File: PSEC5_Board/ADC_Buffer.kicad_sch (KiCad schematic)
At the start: 36 parts, among them IC1 LTC6409IUDB#TRMPBF, IC2 LTC6409IUDB#TRMPBF, IC4 LTC6409IUDB#TRMPBF

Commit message: Added Footprints to Schematic
Added footprints to schematic, should be able to now update the layout design and have all nets be present
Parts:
- C35, C36, C37, C38, C39, C40, C41, C42, C43, C44, C45, C46, C47, C48, C49, C50, C51, C68, C70, C72, C73: footprint (none) -> Capacitor_SMD:C_0603_1608Metric
- IC1, IC2, IC4: footprint footprints:QFN-10_UDB_LIT -> LTC6409IUDB_TRMPBF:QFN-10_UDB_LIT
- R21, R22, R23, R24, R26, R27, R28, R29, R34, R36, R38, R40: footprint (none) -> Resistor_SMD:R_0603_1608Metric
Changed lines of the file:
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@@
 			)
 		)
-		(property "Footprint" ""
+		(property "Footprint" "Resistor_SMD:R_0603_1608Metric"
 			(at 58.166 128.016 90)
 			(effects
@@
 			)
 		)
-		(property "Footprint" ""
+		(property "Footprint" "Capacitor_SMD:C_0603_1608Metric"
 			(at 267.97 123.4948 0)
 			(effects
@@
 			)
 		)
-		(property "Footprint" ""
+		(property "Footprint" "Resistor_SMD:R_0603_1608Metric"
 			(at 36.576 148.336 90)
 			(effects
@@
 			)
 		)
-		(property "Footprint" ""
+		(property "Footprint" "Capacitor_SMD:C_0603_1608Metric"
 			(at 40.64 75.2348 0)
 			(effects
@@
 			)
 		)
-		(property "Footprint" ""
+		(property "Footprint" "Capacitor_SMD:C_0603_1608Metric"
 			(at 55.88 144.4752 0)
 			(effects
@@
 			)
 		)
-		(property "Footprint" ""
+		(property "Footprint" "Capacitor_SMD:C_0603_1608Metric"
 			(at 134.62 131.1148 0)
 			(effects
@@
 			)
 		)
-		(property "Footprint" "footprints:QFN-10_UDB_LIT"
+		(property "Footprint" "LTC6409IUDB_TRMPBF:QFN-10_UDB_LIT"
 			(at 241.3 176.2 0)
 			(effects
@@
 			)
 		)
-		(property "Footprint" ""
+		(property "Footprint" "Capacitor_SMD:C_0603_1608Metric"
 			(at 133.35 86.6648 0)
 			(effects
@@
 			)
 		)
-		(property "Footprint" ""
+		(property "Footprint" "Capacitor_SMD:C_0603_1608Metric"
 			(at 62.23 115.8748 0)
 			(effects
@@
 			)
 		)
-		(property "Footprint" ""
+		(property "Footprint" "Resistor_SMD:R_0603_1608Metric"
 			(at 60.706 73.914 90)
 			(effects
@@
 			)
 		)
-		(property "Footprint" ""
+		(property "Footprint" "Capacitor_SMD:C_0603_1608Metric"
 			(at 133.35 157.7848 0)
 			(effects
@@
 			)
 		)
-		(property "Footprint" ""
+		(property "Footprint" "Capacitor_SMD:C_0603_1608Metric"
 			(at 267.97 112.0648 0)
 			(effects
@@
 			)
 		)
-		(property "Footprint" ""
+		(property "Footprint" "Resistor_SMD:R_0603_1608Metric"
 			(at 45.466 49.276 90)
 			(effects
@@
 			)
 		)
-		(property "Footprint" ""
+		(property "Footprint" "Capacitor_SMD:C_0603_1608Metric"
 			(at 133.35 169.2148 0)
 			(effects
@@
 			)
 		)
-		(property "Footprint" ""
+		(property "Footprint" "Capacitor_SMD:C_0603_1608Metric"
 			(at 133.35 75.2348 0)
 			(effects
@@
 			)
 		)
-		(property "Footprint" ""
+		(property "Footprint" "Capacitor_SMD:C_0603_1608Metric"
 			(at 269.24 73.9648 0)
 			(effects
@@
 			)
 		)
-		(property "Footprint" ""
+		(property "Footprint" "Capacitor_SMD:C_0603_1608Metric"
 			(at 134.62 119.6848 0)
 			(effects
@@
 			)
 		)
-		(property "Footprint" ""
+		(property "Footprint" "Capacitor_SMD:C_0603_1608Metric"
 			(at 62.23 33.3248 0)
 			(effects
@@
 			)
 		)
-		(property "Footprint" ""
+		(property "Footprint" "Capacitor_SMD:C_0603_1608Metric"
 			(at 40.64 157.7848 0)
 			(effects
@@
 			)
 		)
-		(property "Footprint" "footprints:QFN-10_UDB_LIT"
+		(property "Footprint" "LTC6409IUDB_TRMPBF:QFN-10_UDB_LIT"
 			(at 106.68 139.37 0)
 			(effects
@@
 			)
 		)
-		(property "Footprint" ""
+		(property "Footprint" "Resistor_SMD:R_0603_1608Metric"
 			(at 58.166 45.466 90)
 			(effects
@@
 			)
 		)
-		(property "Footprint" ""
+		(property "Footprint" "Resistor_SMD:R_0603_1608Metric"
 			(at 195.326 110.744 90)
 			(effects
@@
 			)
 		)
-		(property "Footprint" ""
+		(property "Footprint" "Capacitor_SMD:C_0603_1608Metric"
 			(at 196.85 70.1548 0)
 			(effects
@@
 			)
 		)
-		(property "Footprint" ""
+		(property "Footprint" "Capacitor_SMD:C_0603_1608Metric"
 			(at 190.5 98.7552 0)
 			(effects
@@
 			)
 		)
-		(property "Footprint" ""
+		(property "Footprint" "Resistor_SMD:R_0603_1608Metric"
 			(at 36.576 65.786 90)
 			(effects
@@
 			)
 		)
-		(property "Footprint" ""
+		(property "Footprint" "Capacitor_SMD:C_0603_1608Metric"
 			(at 175.26 112.0648 0)
 			(effects
@@
 			)
 		)
-		(property "Footprint" ""
+		(property "Footprint" "Resistor_SMD:R_0603_1608Metric"
 			(at 180.086 86.106 90)
 			(effects
@@
 			)
 		)
-		(property "Footprint" ""
+		(property "Footprint" "Resistor_SMD:R_0603_1608Metric"
 			(at 60.706 156.464 90)
 			(effects
@@
 			)
 		)
-		(property "Footprint" ""
+		(property "Footprint" "Resistor_SMD:R_0603_1608Metric"
 			(at 192.786 82.296 90)
 			(effects
@@
 			)
 		)
-		(property "Footprint" ""
+		(property "Footprint" "Capacitor_SMD:C_0603_1608Metric"
 			(at 269.24 85.3948 0)
 			(effects
@@
 			)
 		)
-		(property "Footprint" ""
+		(property "Footprint" "Capacitor_SMD:C_0603_1608Metric"
 			(at 134.62 37.1348 0)
 			(effects
@@
 			)
 		)
-		(property "Footprint" ""
+		(property "Footprint" "Capacitor_SMD:C_0603_1608Metric"
 			(at 55.88 61.9252 0)
 			(effects
@@
 			)
 		)
-		(property "Footprint" ""
+		(property "Footprint" "Capacitor_SMD:C_0603_1608Metric"
 			(at 134.62 48.5648 0)
 			(effects
@@
 			)
 		)
-		(property "Footprint" ""
+		(property "Footprint" "Resistor_SMD:R_0603_1608Metric"
 			(at 171.196 102.616 90)
 			(effects
@@
 			)
 		)
-		(property "Footprint" ""
+		(property "Footprint" "Resistor_SMD:R_0603_1608Metric"
 			(at 45.466 131.826 90)
 			(effects
@@
 			)
 		)
-		(property "Footprint" "footprints:QFN-10_UDB_LIT"
+		(property "Footprint" "LTC6409IUDB_TRMPBF:QFN-10_UDB_LIT"
 			(at 106.68 221.92 0)
 			(effects

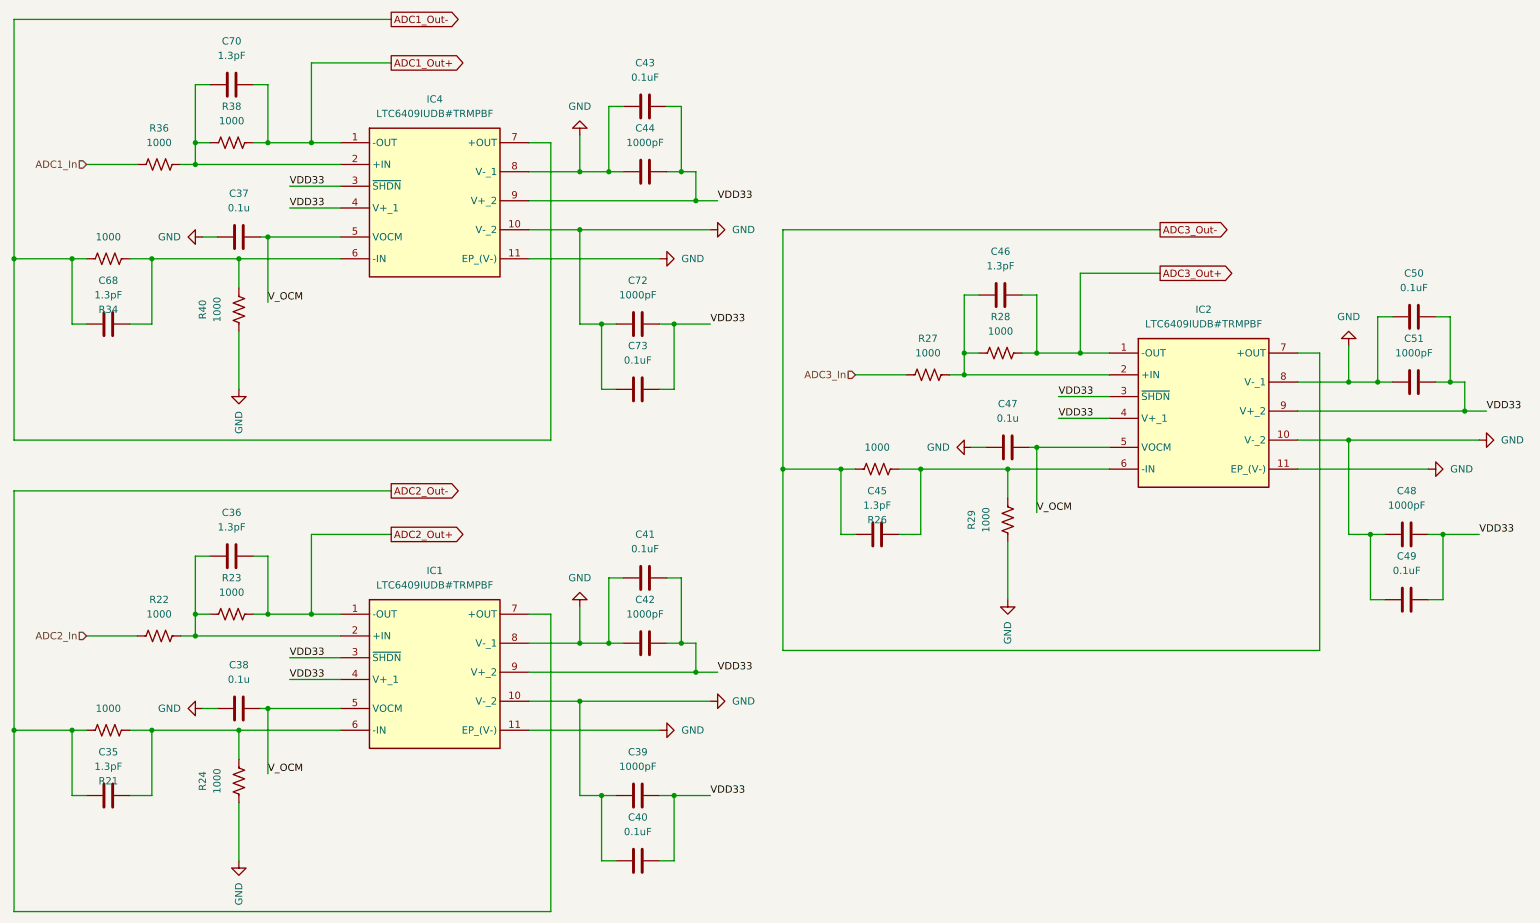
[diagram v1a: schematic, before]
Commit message: DUT Layout Overhaul
Footprints need to be replaced.
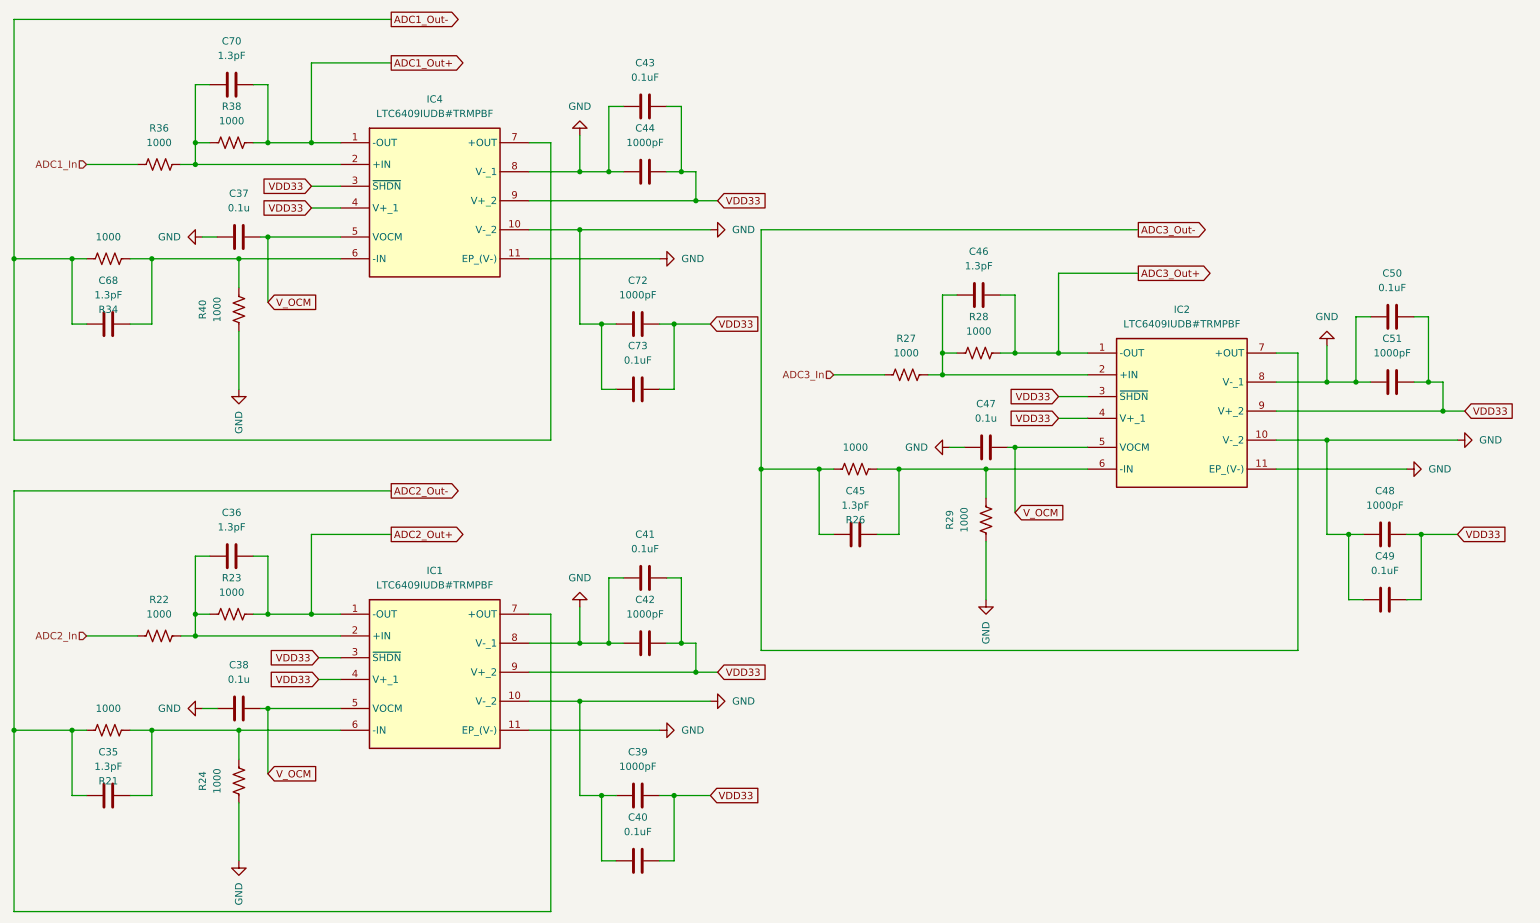
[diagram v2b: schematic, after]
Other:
- moved on the sheet: C45, C46, C47, C48, C49, C50, C51, IC2, R26, R27, R28, R29

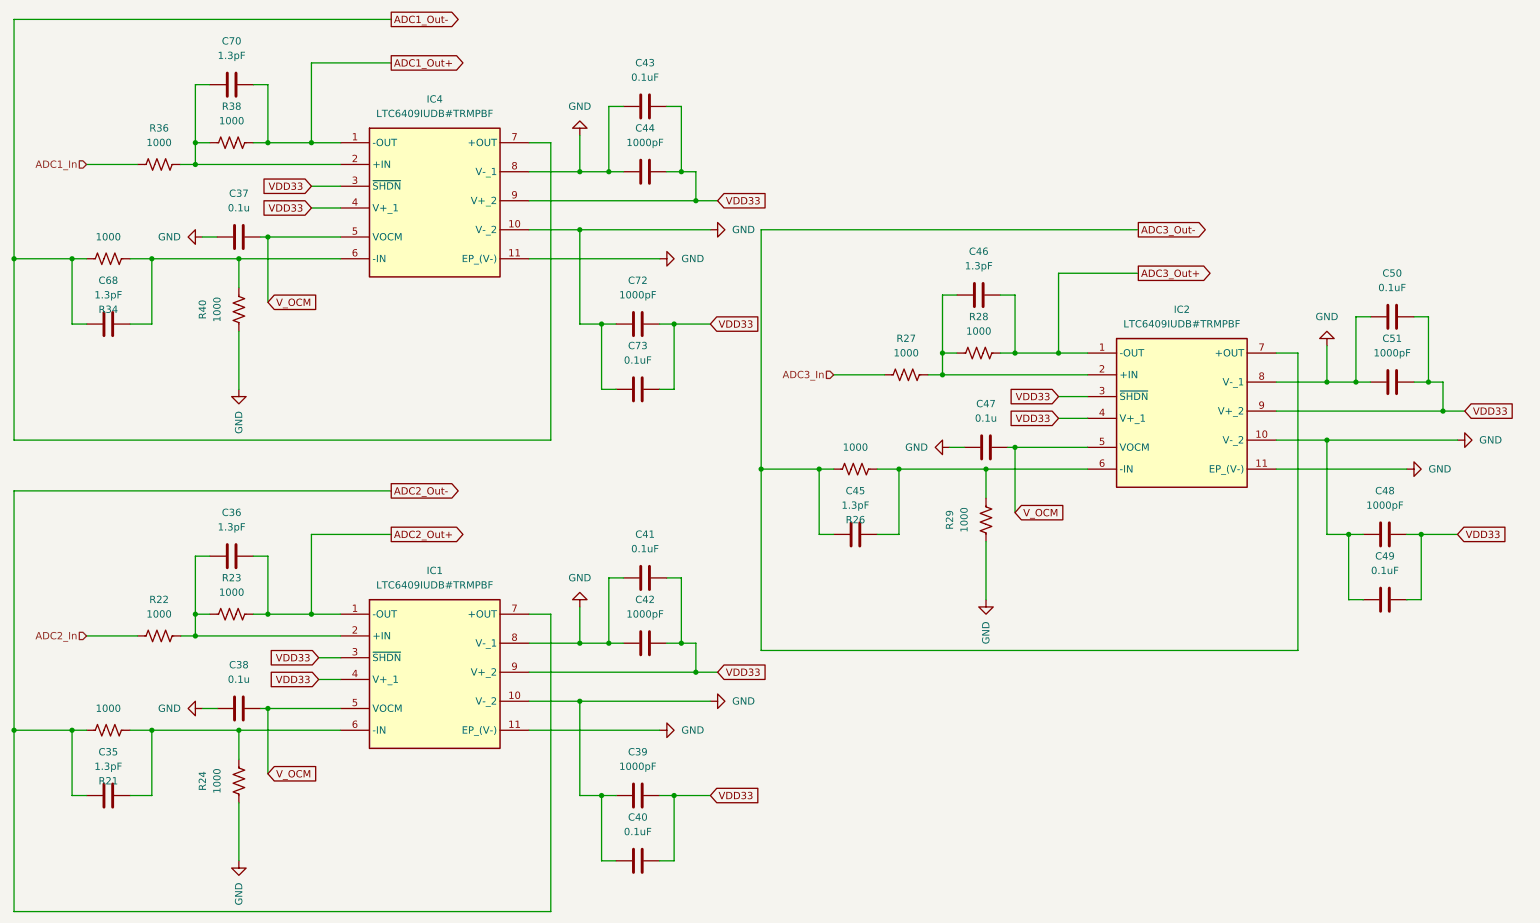
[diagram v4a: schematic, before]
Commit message: DUT v4 Push
Addressed the issues discussed in last week's meeting, cleared ERC errors, still any warnings with Solder Mask.
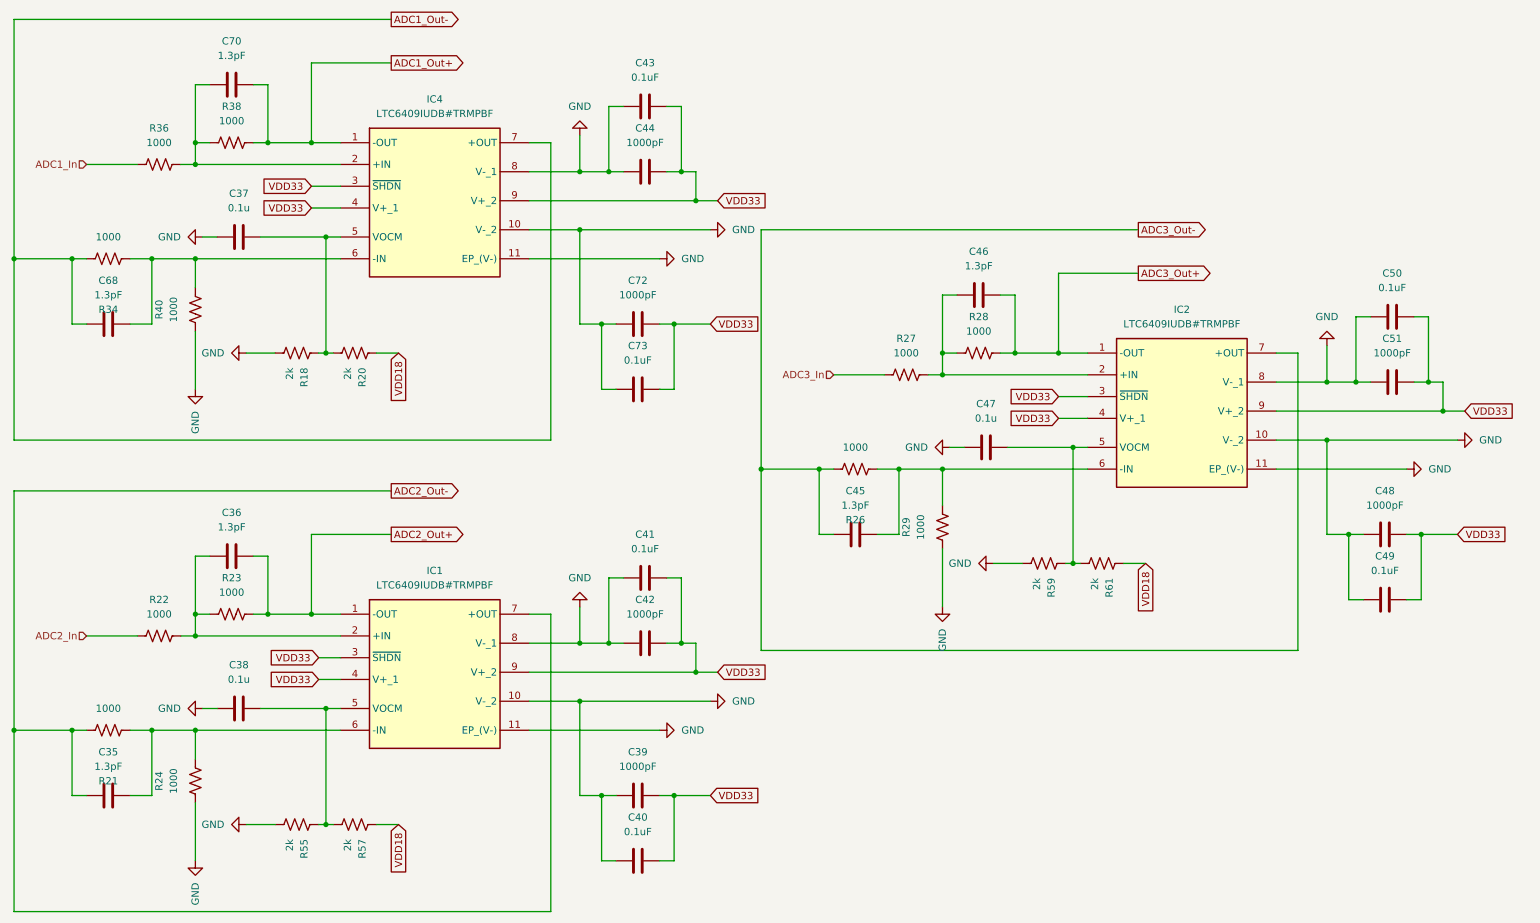
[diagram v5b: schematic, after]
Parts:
- added R18, R20, R55, R57, R59, R61: 2k, Resistor_SMD:R_0603_1608Metric, symbol Device:R_US
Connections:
- net GND: now also R18.2, R55.2, R59.2
- removed net V_OCM: C37.1, C38.1, C47.1, IC1.5 (VOCM), IC2.5 (VOCM), IC4.5 (VOCM)
- new net: C38.1, IC1.5 (VOCM), R55.1, R57.2
- new net: C47.1, IC2.5 (VOCM), R59.1, R61.2
- new net: C37.1, IC4.5 (VOCM), R18.1, R20.2
- new net VDD18: R20.1, R57.1, R61.1
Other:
- moved on the sheet: R24, R29, R40

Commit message: Merge Richmond's production board from JoeModifications into same branch as other boards
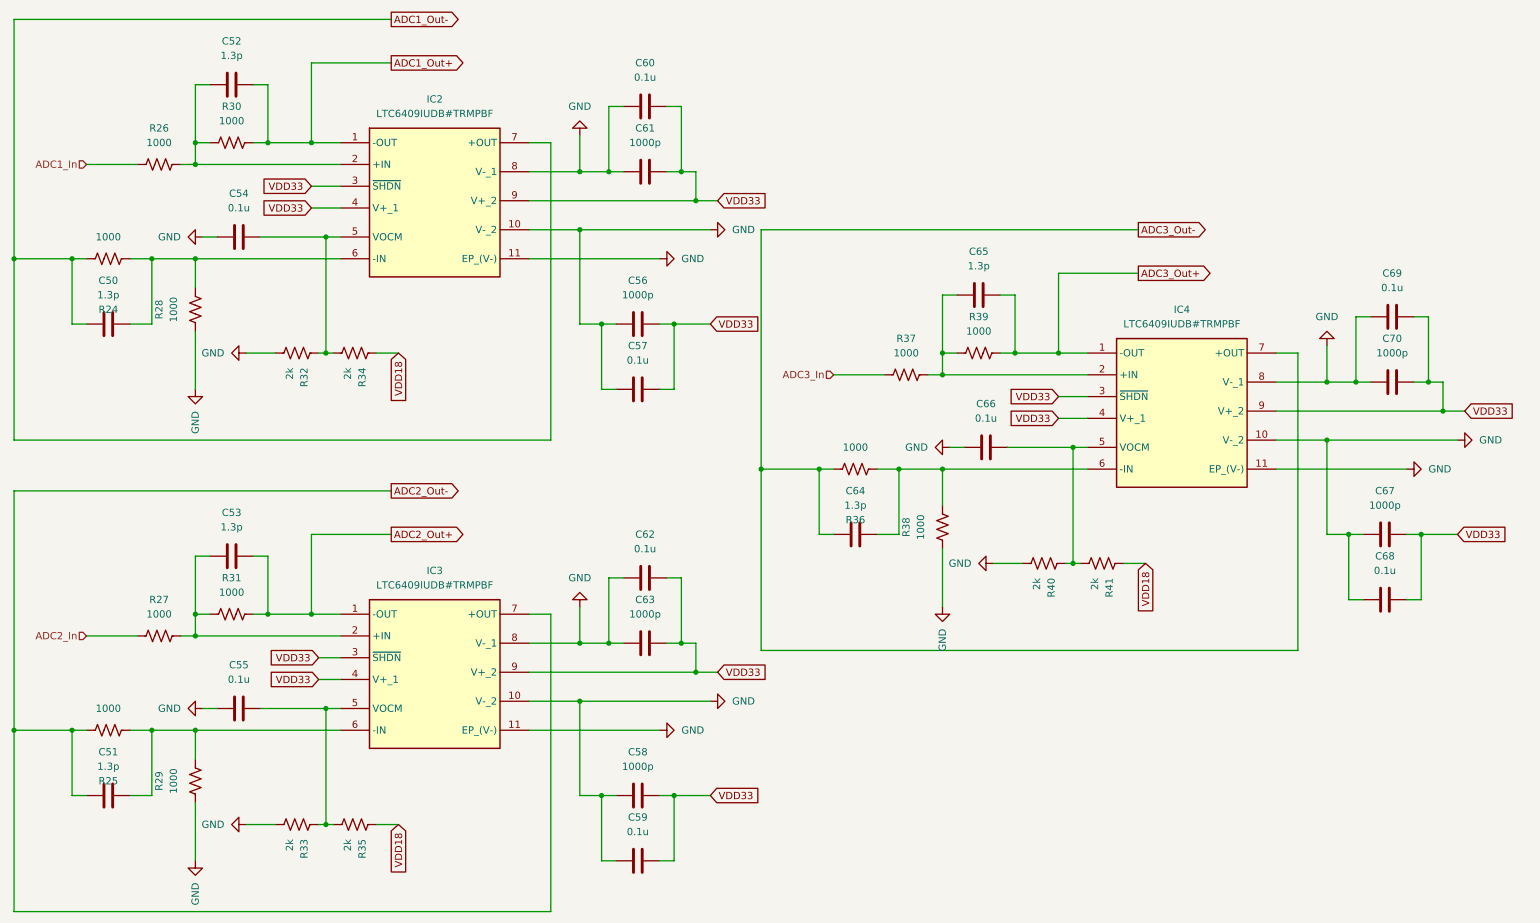
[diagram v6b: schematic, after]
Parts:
- C50: renamed from C68; value 1.3pF -> 1.3p
- C51: renamed from C35; value 1.3pF -> 1.3p
- C52: renamed from C70; value 1.3pF -> 1.3p
- C53: renamed from C36; value 1.3pF -> 1.3p
- C56: renamed from C72; value 1000pF -> 1000p
- C57: renamed from C73; value 0.1uF -> 0.1u
- C58: renamed from C39; value 1000pF -> 1000p
- C59: renamed from C40; value 0.1uF -> 0.1u
- C60: renamed from C43; value 0.1uF -> 0.1u
- C61: renamed from C44; value 1000pF -> 1000p
- C62: renamed from C41; value 0.1uF -> 0.1u
- C63: renamed from C42; value 1000pF -> 1000p
- C64: renamed from C45; value 1.3pF -> 1.3p
- C65: renamed from C46; value 1.3pF -> 1.3p
- C67: renamed from C48; value 1000pF -> 1000p
- C68: renamed from C49; value 0.1uF -> 0.1u
- C69: renamed from C50; value 0.1uF -> 0.1u
- C70: renamed from C51; value 1000pF -> 1000p
- renumbered C37 to C54, C38 to C55, C47 to C66, IC4 to IC2, IC1 to IC3, IC2 to IC4, R34 to R24, R21 to R25, R36 to R26, R22 to R27, R40 to R28, R24 to R29, R38 to R30, R23 to R31, R18 to R32, R55 to R33, R20 to R34, R57 to R35, R26 to R36, R27 to R37, R29 to R38, R28 to R39, R59 to R40, R61 to R41
